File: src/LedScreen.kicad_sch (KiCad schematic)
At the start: 59 parts, among them J1 Micro_SD_Card_Det_Hirose_DM3AT, U1 74HCT245

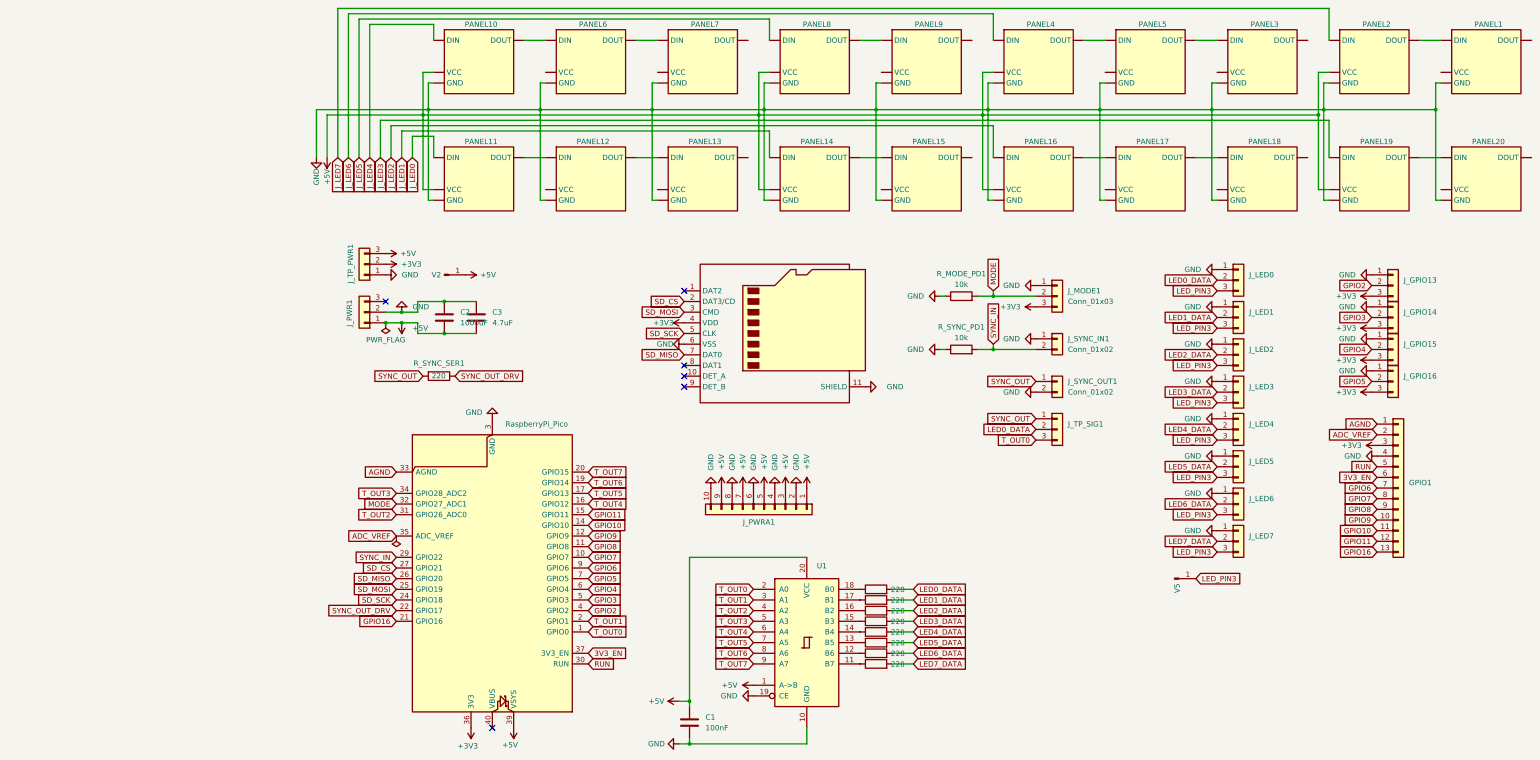
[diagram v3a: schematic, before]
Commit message: Add Main firmware, SDREADD, fseq converter; clean up AI/build artifacts
- arduino_firmware/Main/: new combined firmware
    - Sd.cpp/h: bare-metal SPI SD driver + FAT32 + LSA streaming
    - Leds.cpp/h: 8-lane NeoPixel, pixel mapping, idle blink, current limit
    - UsbStream.cpp/h: xLights USB serial streaming with frame sync
    - Main.ino: setup + loop only
    - Config.h: 20-panel (160×32) layout, safety limits at top
- arduino_firmware/SDREADD/: raw SD diagnostic sketch
- arduino_firmware/RPI-PICO/: cleaned up (SD logic removed, scanner only)
- fseq_to_lsa.py: convert xLights FSEQ → LSA for SD playback (5120 LEDs)
- xlights_project/animation.lsa: pre-converted animation for SD card
- .gitignore: exclude build artifacts, AI harness files, local tools
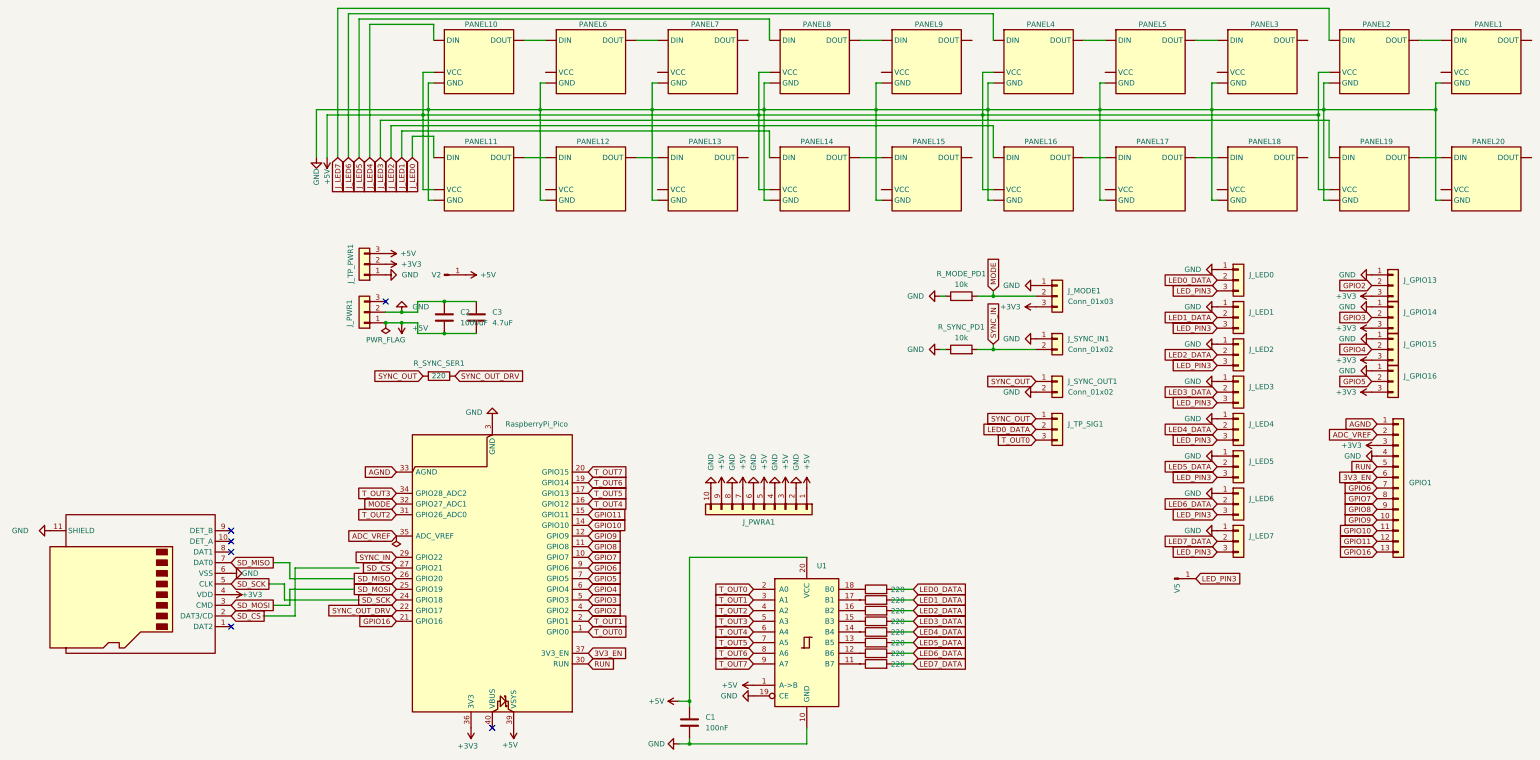
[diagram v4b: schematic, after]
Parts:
- PANEL1, PANEL10, PANEL11, PANEL12, PANEL13, PANEL14, PANEL15, PANEL16, PANEL17, PANEL18, PANEL19, PANEL2, PANEL20, PANEL3, PANEL4, PANEL5, PANEL6, PANEL7, PANEL8, PANEL9: value ~ -> (none)
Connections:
- new net: PANEL8. (DOUT), PANEL9. (DOUT)
- new net: PANEL4. (DOUT), PANEL5. (DOUT)
- new net: PANEL1. (DOUT), PANEL2. (DOUT)
- new net: PANEL19. (DOUT), PANEL20. (DOUT)
- new net: PANEL6. (DOUT), PANEL7. (DOUT)
- new net: PANEL16. (DOUT), PANEL17. (DOUT)
- new net: PANEL12. (DOUT), PANEL13. (DOUT)
- new net: PANEL3. (DOUT), PANEL5. (DOUT)
- new net: PANEL10. (DOUT), PANEL6. (DOUT)
- new net: PANEL17. (DOUT), PANEL18. (DOUT)
- new net: PANEL14. (DOUT), PANEL15. (DOUT)
- new net: PANEL11. (DOUT), PANEL12. (DOUT)
